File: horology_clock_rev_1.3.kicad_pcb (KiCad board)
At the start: 2 copper layers, 100 x 100 mm, 49 parts, among them J1 Conn_01x36, J10 Conn_01x08, J11 Screw_Terminal_01x02, J13 Conn_01x04, J14 Conn_01x10, J15 Conn_01x01, J16 Conn_01x01, J17 Conn_01x01, J2 Conn_01x36, J3 Screw_Terminal_01x02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

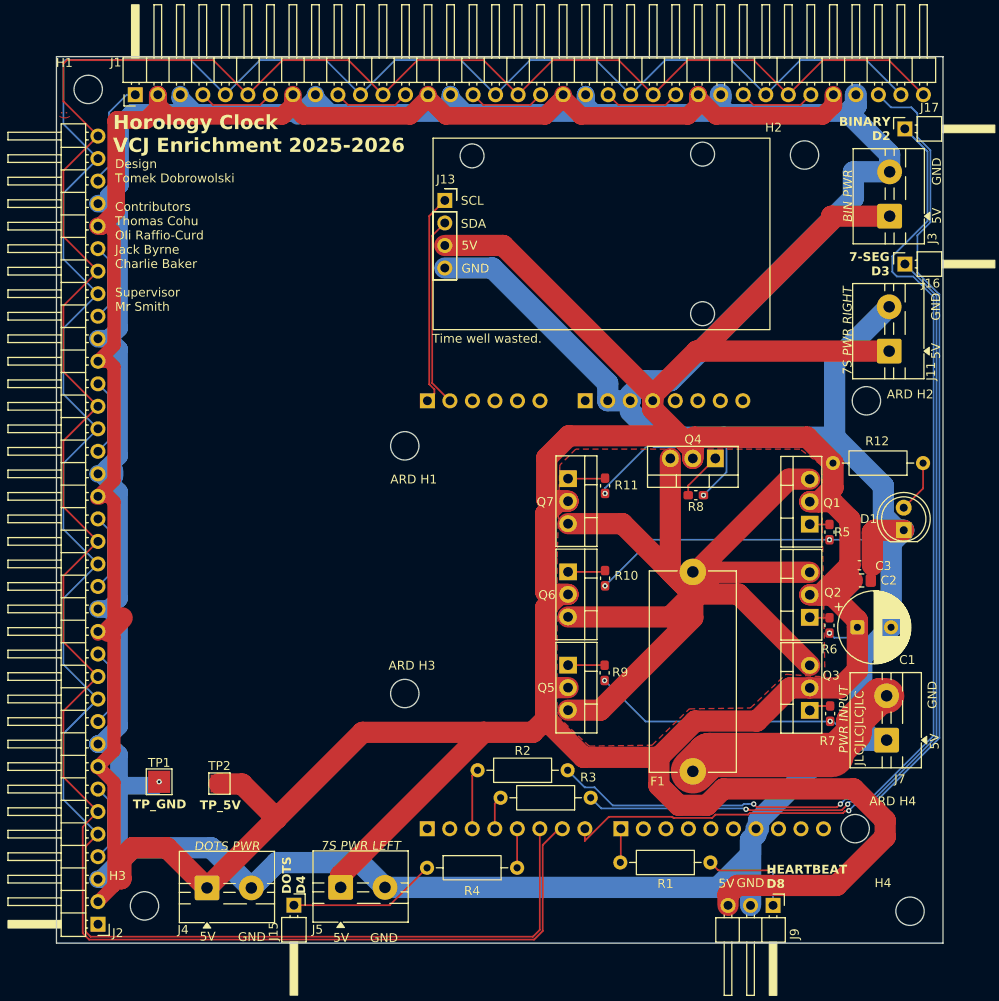
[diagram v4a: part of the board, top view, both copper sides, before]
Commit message: Removed all F.Silk text.
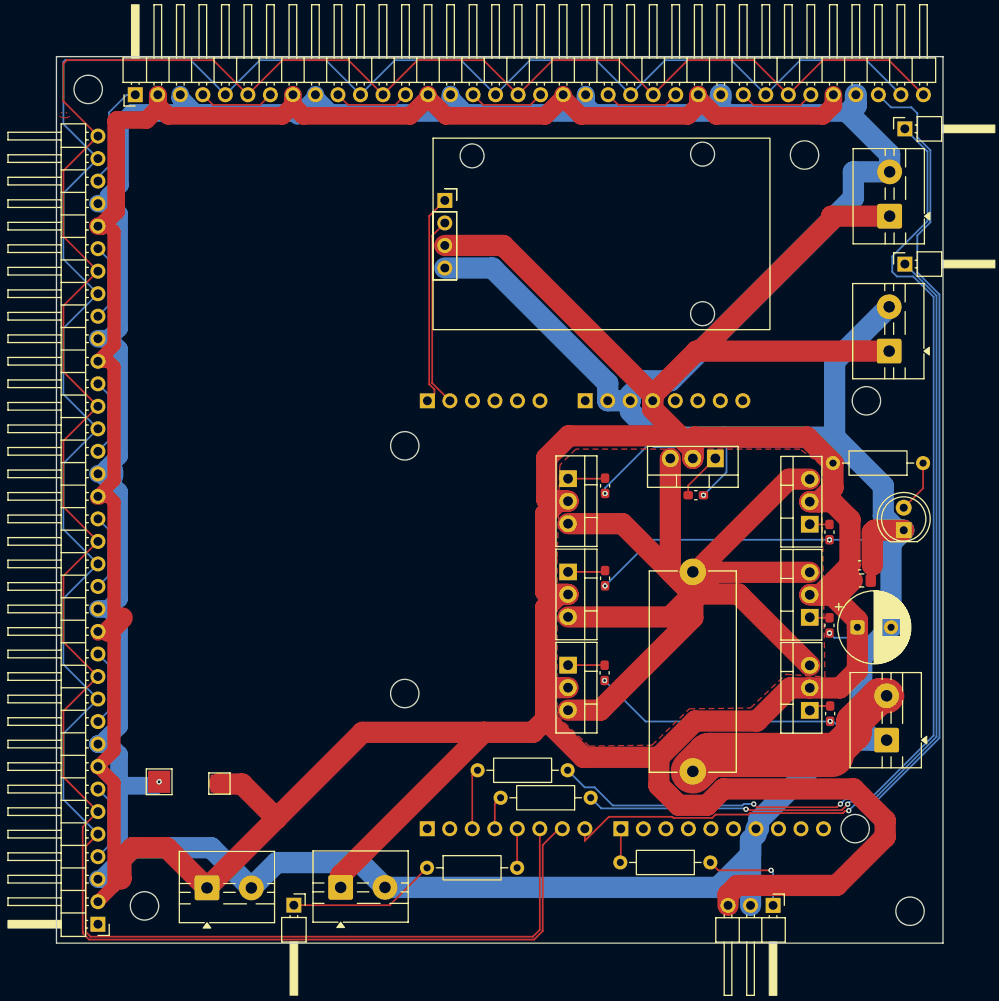
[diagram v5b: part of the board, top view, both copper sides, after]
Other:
- board text removed: "5V"
- board text removed: "7-SEG D3"
- board text removed: "7S PWR LEFT"
- board text removed: "7S PWR RIGHT"
- board text removed: "ARD H1"
- board text removed: "ARD H2"
- board text removed: "ARD H3"
- board text removed: "ARD H4"
- board text removed: "BIN PWR"
- board text removed: "BINARY D2"
- board text removed: "DOTS D4"
- board text removed: "DOTS PWR"
- board text removed: "Design Tomek Dobrowolski Contributors Thomas Cohu Oli Raffio-Curd Jack Byrne Charlie Baker Supervisor Mr Smith"
- board text removed: "GND"
- board text removed: "H4"
- board text removed: "HEARTBEAT D8"
- board text removed: "Horology Clock VCJ Enrichment 2025-2026"
- board text removed: "JLCJLCJLCJLC"
- board text removed: "PWR INPUT"
- board text removed: "SCL"
- board text removed: "SDA"
- board text removed: "TP_5V"
- board text removed: "TP_GND"
- board text removed: "Time well wasted."

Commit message: Removed all B.silk text.
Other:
- board text removed: "ARDUNIO UNO R3"
- board text removed: "J8"
- board text removed: "REV A - It works (probably) March 2026 Victoria College"
- board text removed: "https://github.com/tomekjersey0/horology_clock"
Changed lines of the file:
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@@
 			(at 2.67 -19.377349 0)
 			(layer "B.SilkS")
+			(hide yes)
 			(effects
 				(font
@@
 			(at -2.135 -3.13 0)
 			(layer "B.SilkS")
+			(hide yes)
 			(effects
 				(font
@@
 			(at -2.29 -2.83 180)
 			(layer "B.SilkS")
+			(hide yes)
 			(effects
 				(font
@@
 			(at 2.55 -2.61 0)
 			(layer "B.SilkS")
+			(hide yes)
 			(effects
 				(font
@@
 		)
 	)
-	(gr_text "J8"
-		(at 143.75 90.95 0)
-		(layer "B.SilkS")
-		(effects
-			(font
-				(size 1 1)
-				(thickness 0.15)
-			)
-			(justify left bottom mirror)
-		)
-	)
-	(gr_text "REV A - It works (probably)\nMarch 2026\nVictoria College"
-		(at 87.4 55.975 0)
-		(layer "B.SilkS")
-		(effects
-			(font
-				(size 1 1)
-				(thickness 0.1)
-			)
-			(justify right top mirror)
-		)
-	)
-	(gr_text "https://github.com/tomekjersey0/horology_clock"
-		(at 87 77.615 0)
-		(layer "B.SilkS")
-		(effects
-			(font
-				(size 1 1)
-				(thickness 0.1)
-			)
-			(justify right top mirror)
-		)
-	)
-	(gr_text "ARDUNIO UNO R3"
-		(at 161.35 112.875 0)
-		(layer "B.SilkS")
-		(effects
-			(font
-				(size 1 1)
-				(thickness 0.15)
-			)
-			(justify left bottom mirror)
-		)
-	)
